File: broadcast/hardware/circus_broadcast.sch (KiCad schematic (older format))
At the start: 12 parts

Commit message: Added LM317 to broadcast
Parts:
- removed D? (x2): TSUS4300, symbol TSUS4300
- removed Q?: PMV65XPEA, symbol PMV65XPEA
- removed R? (x3): R, symbol CRCW0402330RFKED
- removed U?: TS321, symbol TS321
- added C? (x6): MC0402X224K6R3CT, symbol MC0402X224K6R3CT
- added Q?: IRLML6244TRPBF, symbol IRLML6244TRPBF
- added R? (x6): 1206, symbol CRCW0402330RFKED
- added U? (x4): LM317DCY, symbol LM317DCY
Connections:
- net labels added: +3.3V, +5V, +BATT, GND, LED_PWM
- wire segments 7 -> 46
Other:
- note added: "LEDs 1.5V @ 30mA"
- note removed: "1.2V @ 30mA"
- moved on the sheet: D?, U?

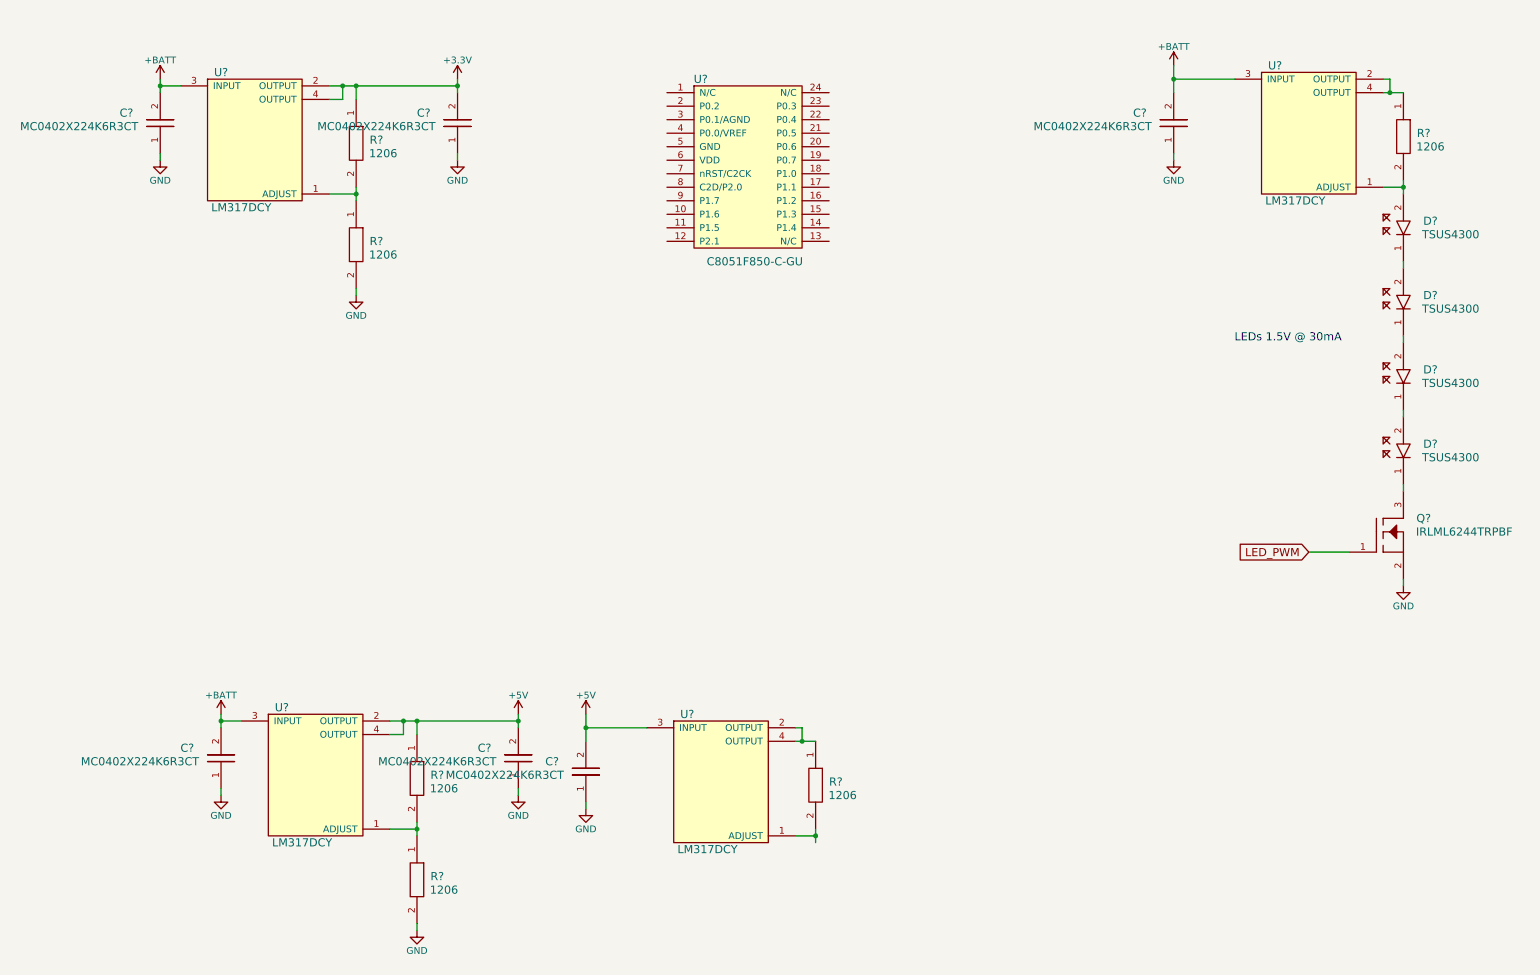
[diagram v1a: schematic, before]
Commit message: Added mcu circuit and format
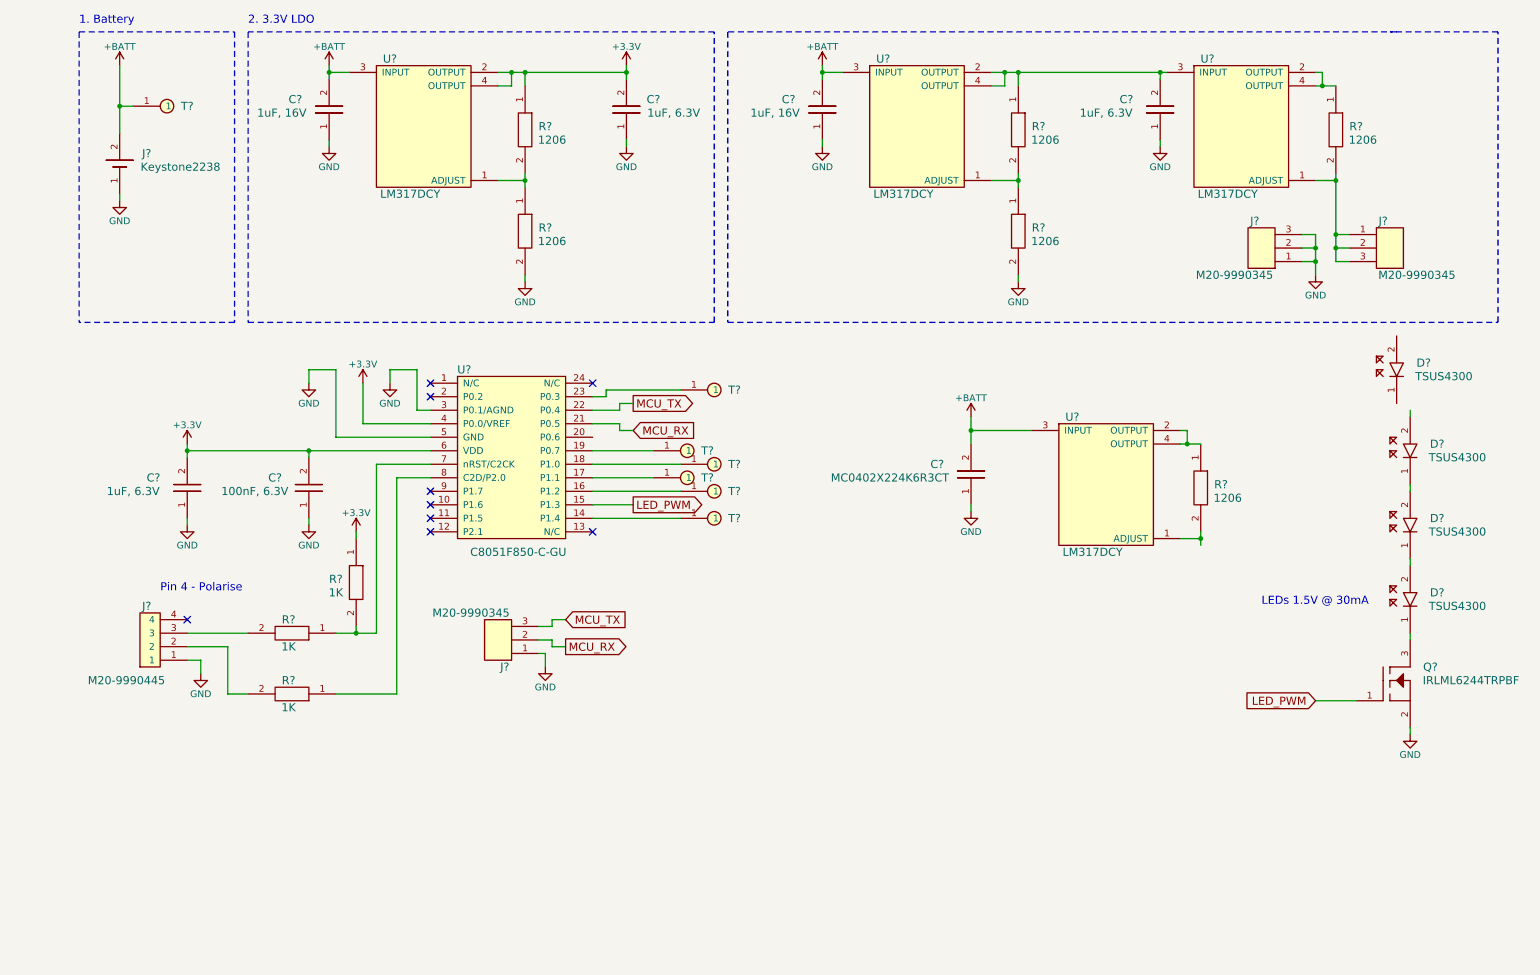
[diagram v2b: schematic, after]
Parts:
- removed C?: MC0402X224K6R3CT, symbol MC0402X224K6R3CT
- added C?: 1uF, 6.3V, symbol MC0402X224K6R3CT
- added C?: 100nF, 6.3V, symbol MC0402X224K6R3CT
- added J?: M20-9990445, symbol M20-9990445
- added J? (x3): M20-9990345, symbol M20-9990345
- added J?: Keystone2238, symbol Keystone2238
- added R? (x3): 1K, symbol CRCW0402330RFKED
- added T? (x7): TestPoint, symbol TestPoint
- C? (x2): value MC0402X224K6R3CT -> 1uF, 16V
- C? (x2): value MC0402X224K6R3CT -> 1uF, 6.3V
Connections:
- net +3V3: now also U?.4 (P0.0/VREF), U?.6 (VDD), C?.2, C?.2, R?.1
- net +BATT: now also J?.2, T?.1
- net GND: now also U?.3 (P0.1/AGND), U?.5 (GND), C?.1, C?.1, J?.1, J?.1, J?.1, J?.1, J?.2, J?.3
- net LED_PWM: now also U?.15 (P1.3)
- net at U?.14 (P1.4): now also T?.1
- net at U?.16 (P1.2): now also T?.1
- net at U?.17 (P1.1): now also T?.1
- net at U?.18 (P1.0): now also T?.1
- net at U?.19 (P0.7): now also T?.1
- net MCU_RX: now reaches U?.21 (P0.5)
- net MCU_RX: now also J?.2
- net MCU_TX: now reaches U?.22 (P0.4)
- net MCU_TX: now also J?.3
- net at U?.23 (P0.3): now also T?.1
- net at U?.7 (nRST/C2CK): now also R?.1, R?.2
- net at U?.8 (C2D/P2.0): now also R?.1
- net at D?.1: no longer D?.2
- net at R?.2, U?.1 (ADJUST): no longer D?.2
- net at R?.2, U?.1 (ADJUST): now also J?.1, J?.2, J?.3
- net +5V: no longer names the net of C?.2, R?.1, U?.2 (OUTPUT), U?.3 (INPUT), U?.4 (OUTPUT)
- new net: J?.3, R?.2
- new net: J?.2, R?.2
- no-connect marks 0 -> 9
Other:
- note added: "1. Battery"
- note added: "2. 3.3V LDO"
- note added: "Pin 4 - Polarise"
- moved on the sheet: C?, D?, Q?, R?, U?

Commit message: Added designators and values
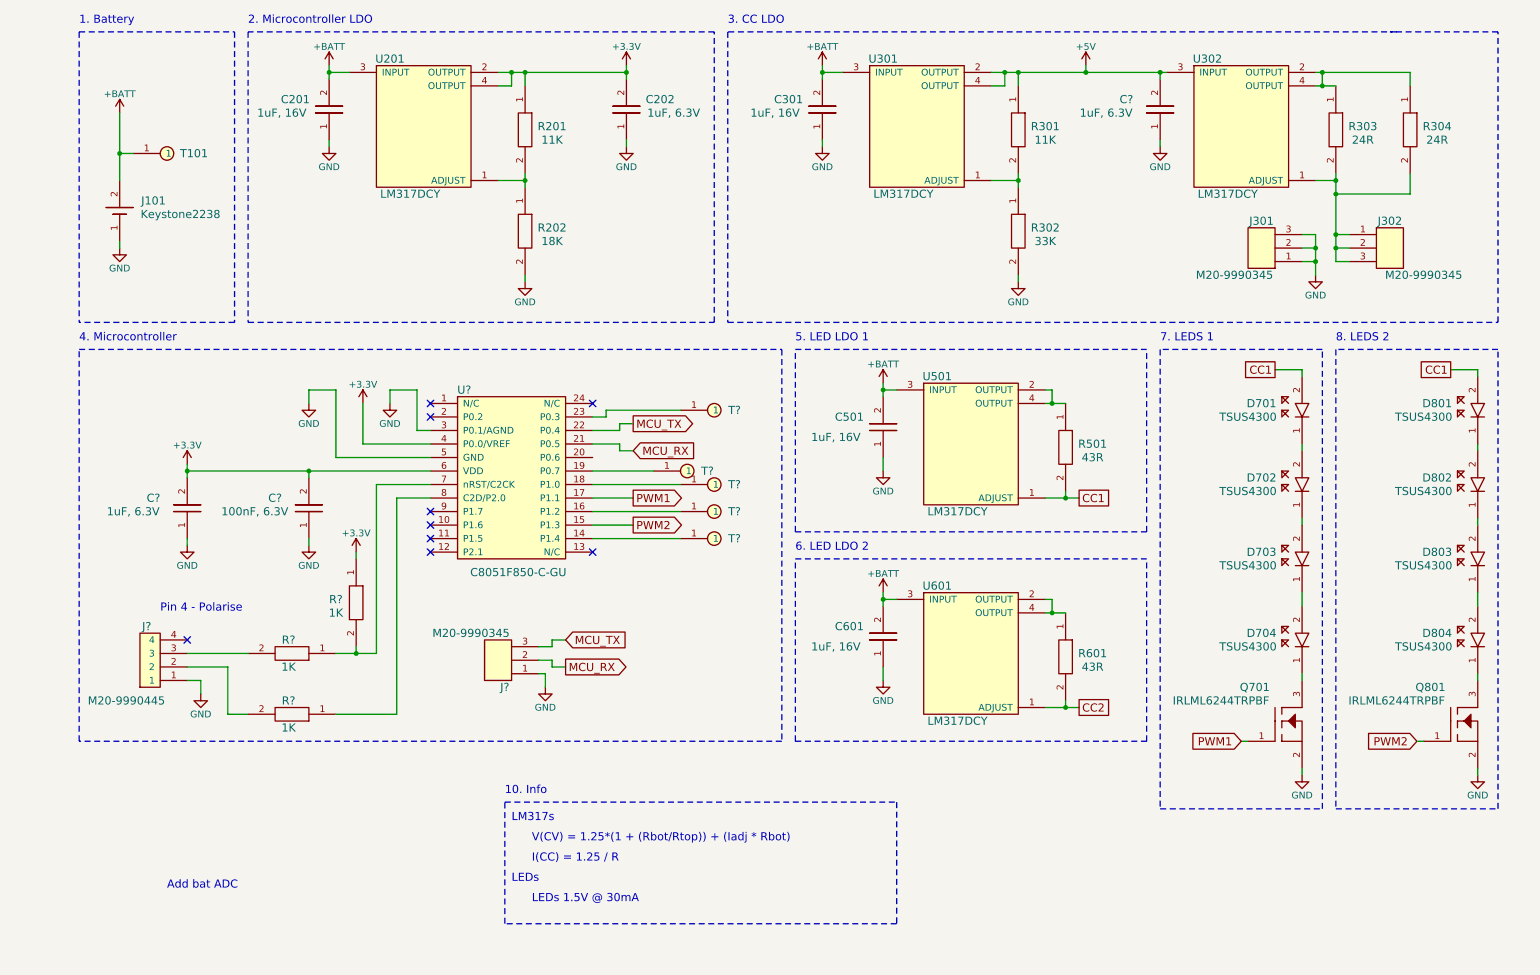
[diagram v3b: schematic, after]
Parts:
- removed D? (x3): TSUS4300, symbol TSUS4300
- removed T?: TestPoint, symbol TestPoint
- added C501: 1uF, 16V, symbol MC0402X224K6R3CT
- added D701, D702, D703, D801, D802, D803, D804: TSUS4300, symbol TSUS4300
- added Q801: IRLML6244TRPBF, symbol IRLML6244TRPBF
- added R304: 24R, symbol CRCW0402330RFKED
- added R501: 43R, symbol CRCW0402330RFKED
- added U501: LM317DCY, symbol LM317DCY
- C601: renamed from C?; value MC0402X224K6R3CT -> 1uF, 16V
- R201, R301: renamed from R?; value 1206 -> 11K
- R202: renamed from R?; value 1206 -> 18K
- R302: renamed from R?; value 1206 -> 33K
- R303: renamed from R?; value 1206 -> 24R
- R601: renamed from R?; value 1206 -> 43R
- gave numbers to parts that had none: 13
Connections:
- net +BATT: now also C501.2, U501.3 (INPUT)
- net GND: now also C501.1, Q801.2
- net PWM1: now reaches U?.17 (P1.1)
- net PWM1: now also Q701.1
- net at D704.2: now also D703.1
- net CC2: now reaches R601.2, U601.1 (ADJUST)
- net +5V: now reaches C?.2, R301.1, U301.2 (OUTPUT), U301.4 (OUTPUT), U302.3 (INPUT)
- net at R303.1, U302.2 (OUTPUT), U302.4 (OUTPUT): now also R304.1
- net at J302.1, J302.2, J302.3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: now also R304.2
- net LED_PWM renamed PWM2
- net PWM2: now also Q801.1; no longer Q701.1
- new net: R501.1, U501.2 (OUTPUT), U501.4 (OUTPUT)
- new net: D702.1, D703.2
- new net: D701.1, D702.2
- new net: D804.1, Q801.3
- new net: D803.1, D804.2
- new net: D802.1, D803.2
- new net: D801.1, D802.2
- new net CC1: D701.2, D801.2, R501.2, U501.1 (ADJUST)
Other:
- note added: "10. Info"
- note added: "2. Microcontroller LDO"
- note added: "3. CC LDO"
- note added: "4. Microcontroller"
- note added: "5. LED LDO 1"
- note added: "6. LED LDO 2"
- note added: "7. LEDS 1"
- note added: "8. LEDS 2"
- note added: "Add bat ADC"
- note added: "I(CC) = 1.25 / R"
- note added: "LEDs\n"
- note added: "LM317s"
- note added: "V(CV) = 1.25*(1 + (Rbot/Rtop)) + (Iadj * Rbot)"
- note removed: "2. 3.3V LDO"
- moved on the sheet: C601, C?, D704, J101, J?, Q701, R601, R?, T101, T?, U601, U?

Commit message: Added ADC, LEDS and passes erc
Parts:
- removed T? (x3): TestPoint, symbol TestPoint
- added D901: KPA-1606CGCK(GREEN), symbol KPA-1606CGCK(GREEN)
- added D902: KPA-1606ECR(RED), symbol KPA-1606ECR(RED)
- added R901: 750R, symbol CRCW0402330RFKED
- added R902: 270R, symbol CRCW0402330RFKED
- added R903: 33R, symbol CRCW0402330RFKED
- added R904: 39R, symbol CRCW0402330RFKED
- gave numbers to parts that had none: 11
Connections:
- net +BATT: now also R901.2
- net CC1: no longer D801.2
- net CC2: now also D801.2
- net GND: now also D901.1, D902.1, R902.2
- net 0.26ADC: now reaches U401.14 (P1.4)
- net 0.26ADC: now also R901.1, R902.1
- net LEDR: now reaches U401.16 (P1.2)
- net LEDR: now also R904.2
- net LEDG: now reaches U401.18 (P1.0)
- net LEDG: now also R903.1
- new net: D901.2, R903.2
- new net: D902.2, R904.1
- no-connect marks 9 -> 10
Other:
- note added: "9. Measure and LEDs"
- note removed: "Add bat ADC"

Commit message: Associate, footprint and start placement
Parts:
- C201, C202, C301, C302, C401, C501, C601: footprint (none) -> circus_broadcast:0603
- C402, R201, R202, R301, R302, R303, R304, R401, R402, R403, R501, R601, R901, R902, R903, R904: footprint (none) -> circus_agent:0402
- D701, D702, D703, D704, D801, D802, D803, D804: footprint (none) -> circus_broadcast:TSUS4300
- D901, D902: footprint (none) -> circus_agent:KPA
- J301, J302, J402: footprint (none) -> circus_agent:M20-9990345
- Q701, Q801: footprint (none) -> circus_agent:IRLML6244TRPBF
- T101, T401, T402: footprint (none) -> circus_broadcast:TestPoint
- U201, U301, U302, U501, U601: footprint (none) -> circus_broadcast:LM317DCY
- U401: footprint (none) -> circus_agent:C8051F850-C-GU

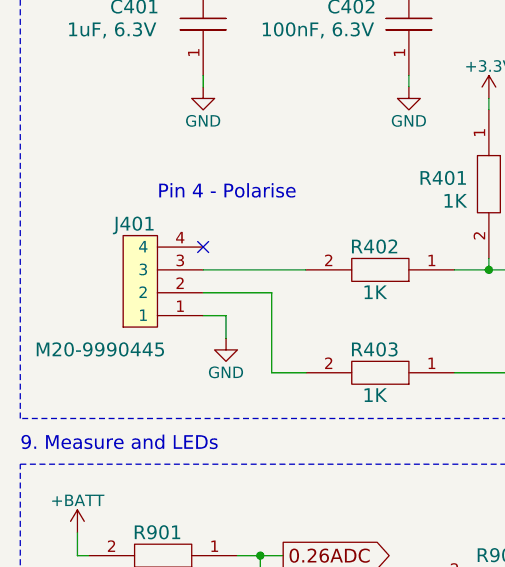
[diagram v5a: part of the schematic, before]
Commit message: All all footprints and made 0.1 inch headers bigger
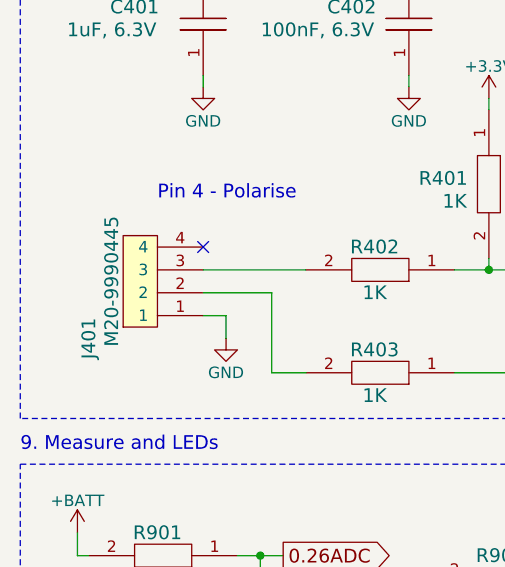
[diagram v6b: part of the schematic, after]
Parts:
- J101: footprint (none) -> circus_broadcast:Keystone2238
- J401: footprint (none) -> circus_broadcast:M20-9990445
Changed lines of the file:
@@
 Wire Wire Line
 	2650 4600 2650 4550
-$Comp
-L M20-9990445 J401
-U 1 1 5BB3F036
-P 1400 5550
-F 0 "J401" V 1850 5850 60  0000 C CNN
-F 1 "M20-9990445" V 1300 6000 60  0000 C CNN
-F 2 "" H 1400 5550 60  0001 C CNN
-F 3 "" H 1400 5550 60  0001 C CNN
-	1    1400 5550
-	0    -1   -1   0
-$EndComp
 NoConn ~ 1400 5200
 $Comp
@@
 F 0 "J101" H 1150 2550 60  0000 C CNN
 F 1 "Keystone2238" H 1350 2450 60  0000 C CNN
-F 2 "" H 800 2250 60  0001 C CNN
+F 2 "circus_broadcast:Keystone2238" H 800 2250 60  0001 C CNN
 F 3 "" H 800 2250 60  0001 C CNN
 	1    800  2250
@@
 	1    0    0    -1
 $EndComp
+$Comp
+L M20-9990445 J401
+U 1 1 5BE0DCD3
+P 1400 5550
+F 0 "J401" H 1350 6050 60  0000 C CNN
+F 1 "M20-9990445" H 1600 5950 60  0000 C CNN
+F 2 "circus_broadcast:M20-9990445" H 1400 5550 60  0001 C CNN
+F 3 "" H 1400 5550 60  0001 C CNN
+	1    1400 5550
+	0    -1   -1   0
+$EndComp
 $EndSCHEMATC
